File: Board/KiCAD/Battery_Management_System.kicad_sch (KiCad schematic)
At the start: 19 parts, among them J10 Conn_01x02, J11 Conn_01x02, J12 Conn_01x02, J13 Conn_01x02, J5 Conn_01x03, J6 Conn_01x03, J7 Conn_01x05, J8 Conn_01x02, J9 Conn_01x02

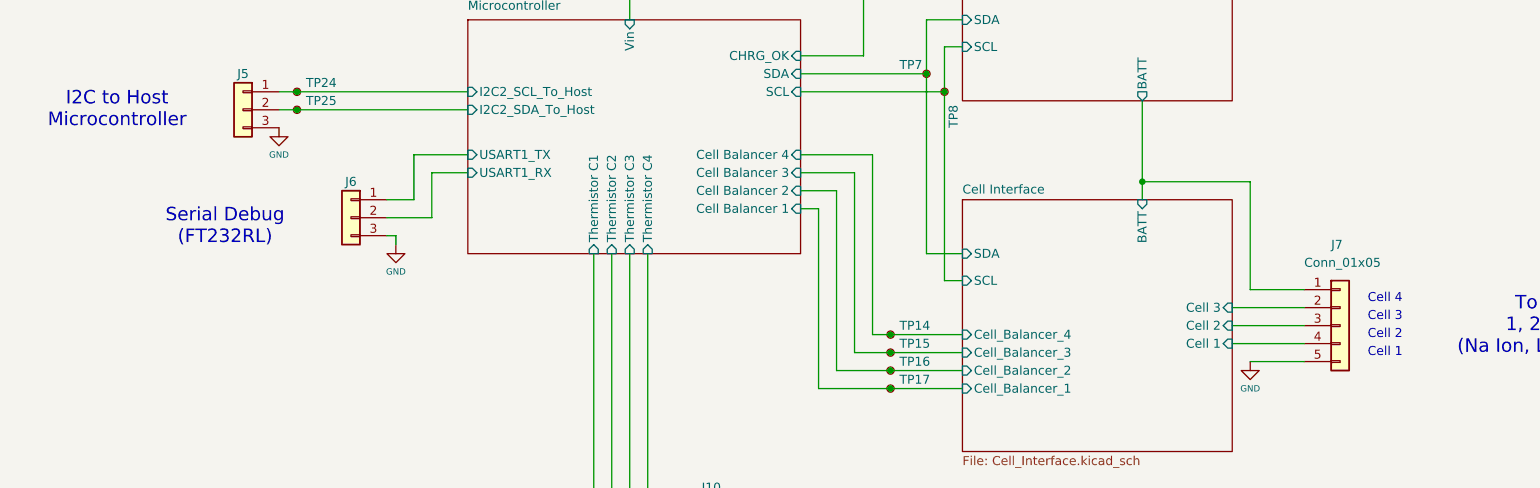
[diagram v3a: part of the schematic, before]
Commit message: Optimized PCB
PCB new dimensions:
43 x 53 mm
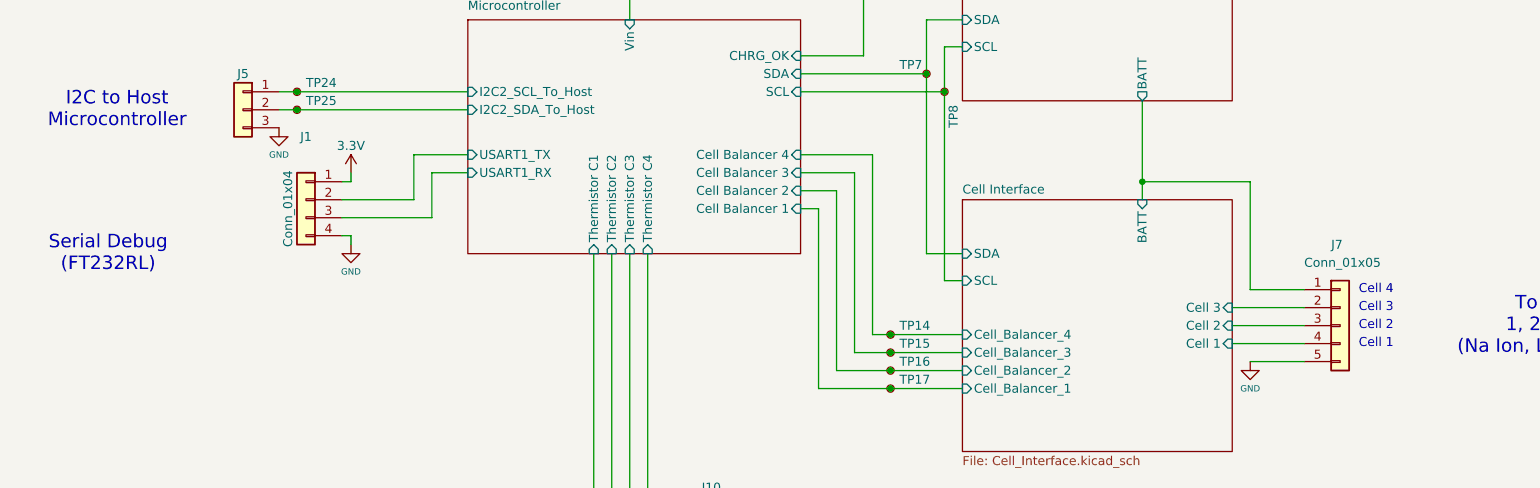
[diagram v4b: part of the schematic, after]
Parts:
- removed J6: Conn_01x03, Connector_PinHeader_2.54mm:PinHeader_1x03_P2.54mm_Vertical, symbol Connector_Generic:Conn_01x03
- added J1: Conn_01x04, Connector_PinHeader_2.54mm:PinHeader_1x04_P2.54mm_Vertical, symbol Connector_Generic:Conn_01x04
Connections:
- net GND: now also J1.4 (Pin_4)
- net Microcontroller/USART1_RX: now also J1.3 (Pin_3)
- net Microcontroller/USART1_TX: now also J1.2 (Pin_2)
- new net 3.3V: J1.1 (Pin_1)
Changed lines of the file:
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@@
 	(text "Cell 3"
 		(exclude_from_sim no)
-		(at 208.28 119.38 0)
+		(at 207.01 118.11 0)
 		(effects
 			(font
@@
 	(text "Cell 4\n"
 		(exclude_from_sim no)
-		(at 208.28 116.84 0)
+		(at 207.01 115.57 0)
 		(effects
 			(font
@@
 	(text "Cell 2"
 		(exclude_from_sim no)
-		(at 208.28 121.92 0)
+		(at 207.01 120.65 0)
 		(effects
 			(font
@@
 	(text "Serial Debug\n(FT232RL)"
 		(exclude_from_sim no)
-		(at 44.45 106.68 0)
+		(at 27.94 110.49 0)
 		(effects
 			(font
@@
 	(text "Cell 1\n"
 		(exclude_from_sim no)
-		(at 208.28 124.46 0)
+		(at 207.01 123.19 0)
 		(effects
 			(font
@@
 	(wire
 		(pts
+			(xy 62.23 99.06) (xy 62.23 100.33)
+		)
+		(stroke
+			(width 0)
+			(type default)
+		)
+	)
+	(wire
+		(pts
 			(xy 189.23 115.57) (xy 189.23 100.33)
 		)
@@
 	(wire
 		(pts
-			(xy 67.31 105.41) (xy 73.66 105.41)
+			(xy 60.96 105.41) (xy 73.66 105.41)
 		)
 		(stroke
@@
 	(wire
 		(pts
-			(xy 68.58 109.22) (xy 68.58 107.95)
+			(xy 62.23 109.22) (xy 62.23 107.95)
 		)
 		(stroke
@@
 	(wire
 		(pts
-			(xy 68.58 107.95) (xy 67.31 107.95)
+			(xy 62.23 107.95) (xy 60.96 107.95)
 		)
 		(stroke
@@
 	(wire
 		(pts
+			(xy 62.23 100.33) (xy 60.96 100.33)
+		)
+		(stroke
+			(width 0)
+			(type default)
+		)
+	)
+	(wire
+		(pts
 			(xy 173.99 88.9) (xy 173.99 100.33)
 		)
@@
 	(wire
 		(pts
-			(xy 67.31 102.87) (xy 71.12 102.87)
+			(xy 60.96 102.87) (xy 71.12 102.87)
 		)
 		(stroke
@@
 	(symbol
 		(lib_id "power:GND")
-		(at 68.58 109.22 0)
+		(at 62.23 109.22 0)
 		(unit 1)
 		(exclude_from_sim no)
@@
 		(dnp no)
 		(property "Reference" "#PWR077"
-			(at 68.58 115.57 0)
+			(at 62.23 115.57 0)
 			(effects
 				(font
@@
 		)
 		(property "Value" "GND"
-			(at 68.58 113.03 0)
+			(at 62.23 113.03 0)
 			(effects
 				(font
@@
 		)
 		(property "Footprint" ""
-			(at 68.58 109.22 0)
+			(at 62.23 109.22 0)
 			(effects
 				(font
@@
 		)
 		(property "Datasheet" ""
-			(at 68.58 109.22 0)
+			(at 62.23 109.22 0)
 			(effects
 				(font
@@
 		)
 		(property "Description" "Power symbol creates a global label with name \"GND\" , ground"
-			(at 68.58 109.22 0)
+			(at 62.23 109.22 0)
 			(effects
 				(font
@@
 	)
 	(symbol
+		(lib_id "Connector_Generic:Conn_01x04")
+		(at 55.88 102.87 0)
+		(mirror y)
+		(unit 1)
+		(exclude_from_sim no)
+		(in_bom yes)
+		(on_board yes)
+		(dnp no)
+		(property "Reference" "J1"
+			(at 55.88 93.98 0)
+			(effects
+				(font
+					(size 1.27 1.27)
+				)
+			)
+		)
+		(property "Value" "Conn_01x04"
+			(at 53.34 104.14 90)
+			(effects
+				(font
+					(size 1.27 1.27)
+				)
+			)
+		)
+		(property "Footprint" "Connector_PinHeader_2.54mm:PinHeader_1x04_P2.54mm_Vertical"
+			(at 55.88 102.87 0)
+			(effects
+				(font
+					(size 1.27 1.27)
+				)
+				(hide yes)
+			)
+		)
+		(property "Datasheet" "~"
+			(at 55.88 102.87 0)
+			(effects
+				(font
+					(size 1.27 1.27)
+				)
+				(hide yes)
+			)
+		)
+		(property "Description" "Generic connector, single row, 01x04, script generated (kicad-library-utils/schlib/autogen/connector/)"
+			(at 55.88 102.87 0)
+			(effects
+				(font
+					(size 1.27 1.27)
+				)
+				(hide yes)
+			)
+		)
+		(pin "3"
+		)
+		(pin "4"
+		)
+		(pin "1"
+		)
+		(pin "2"
+		)
+		(instances
+			(project ""
+				(path "/1ea1a1f5-2618-4570-85b6-e164c8f0e76f"
+					(reference "J1")
+					(unit 1)
+				)
+			)
+		)
+	)
+	(symbol
 		(lib_id "Connector_Generic:Conn_01x02")
 		(at 113.03 146.05 0)
@@
 	)
 	(symbol
-		(lib_id "Connector_Generic:Conn_01x03")
-		(at 62.23 105.41 0)
-		(mirror y)
-		(unit 1)
-		(exclude_from_sim no)
-		(in_bom yes)
-		(on_board yes)
-		(dnp no)
-		(property "Reference" "J6"
-			(at 62.23 100.33 0)
-			(effects
-				(font
-					(size 1.27 1.27)
-				)
-			)
-		)
-		(property "Value" "Conn_01x03"
-			(at 62.23 99.06 0)
-			(effects
-				(font
-					(size 1.27 1.27)
-				)
-				(hide yes)
-			)
-		)
-		(property "Footprint" "Connector_PinHeader_2.54mm:PinHeader_1x03_P2.54mm_Vertical"
-			(at 62.23 105.41 0)
-			(effects
-				(font
-					(size 1.27 1.27)
-				)
-				(hide yes)
-			)
-		)
-		(property "Datasheet" "~"
-			(at 62.23 105.41 0)
-			(effects
-				(font
-					(size 1.27 1.27)
-				)
-				(hide yes)
-			)
-		)
-		(property "Description" "Generic connector, single row, 01x03, script generated (kicad-library-utils/schlib/autogen/connector/)"
-			(at 62.23 105.41 0)
-			(effects
-				(font
-					(size 1.27 1.27)
-				)
-				(hide yes)
-			)
-		)
-		(property "Availability" ""
-			(at 62.23 105.41 0)
-			(effects
-				(font
-					(size 1.27 1.27)
-				)
-			)
-		)
-		(property "Check_prices" ""
-			(at 62.23 105.41 0)
-			(effects
-				(font
-					(size 1.27 1.27)
-				)
-			)
-		)
-		(property "Description_1" ""
-			(at 62.23 105.41 0)
-			(effects
-				(font
-					(size 1.27 1.27)
-				)
-			)
-		)
-		(property "MANUFACTURER" ""
-			(at 62.23 105.41 0)
-			(effects
-				(font
-					(size 1.27 1.27)
-				)
-			)
-		)
-		(property "MAXIMUM_PACKAGE_HEIGHT" ""
-			(at 62.23 105.41 0)
-			(effects
-				(font
-					(size 1.27 1.27)
-				)
-			)
-		)
-		(property "PARTREV" ""
-			(at 62.23 105.41 0)
-			(effects
-				(font
-					(size 1.27 1.27)
-				)
-			)
-		)
-		(property "Package" "61300311121"
-			(at 55.372 112.522 0)
-			(effects
-				(font
-					(size 1.27 1.27)
-				)
-				(hide yes)
-			)
-		)
-		(property "Price" ""
-			(at 62.23 105.41 0)
-			(effects
-				(font
-					(size 1.27 1.27)
-				)
-			)
-		)
-		(property "SNAPEDA_PN" ""
-			(at 62.23 105.41 0)
-			(effects
-				(font
-					(size 1.27 1.27)
-				)
-			)
-		)
-		(property "STANDARD" ""
-			(at 62.23 105.41 0)
-			(effects
-				(font
-					(size 1.27 1.27)
-				)
-			)
-		)
-		(property "SnapEDA_Link" ""
-			(at 62.23 105.41 0)
-			(effects
-				(font
-					(size 1.27 1.27)
-				)
-			)
-		)
-		(property "MFR" "Würth Elektronik"
-			(at 61.468 97.79 0)
-			(effects
-				(font
-					(size 1.27 1.27)
-				)
-				(hide yes)
-			)
-		)
-		(property "MPN" "732-5316-ND"
-			(at 62.23 114.808 0)
-			(effects
-				(font
-					(size 1.27 1.27)
-				)
-				(hide yes)
-			)
-		)
-		(pin "2"
-		)
-		(pin "3"
-		)
-		(pin "1"
-		)
-		(instances
-			(project "Battery_Management_System"
-				(path "/1ea1a1f5-2618-4570-85b6-e164c8f0e76f"
-					(reference "J6")
-					(unit 1)
-				)
-			)
-		)
-	)
-	(symbol
 		(lib_id "Connector_Generic:Conn_01x02")
 		(at 113.03 172.72 0)
@@
 					(unit 1)
 				)
+			)
+		)
+	)
+	(symbol
+		(lib_id "power:VCC")
+		(at 62.23 99.06 0)
+		(unit 1)
+		(exclude_from_sim no)
+		(in_bom yes)
+		(on_board yes)
+		(dnp no)
+		(property "Reference" "#PWR042"
+			(at 62.23 102.87 0)
+			(effects
+				(font
+					(size 1.27 1.27)
+				)
+				(hide yes)
+			)
+		)
+		(property "Value" "3.3V"
+			(at 62.23 95.25 0)
+			(effects
+				(font
+					(size 1.27 1.27)
+				)
+			)
+		)
+		(property "Footprint" ""
+			(at 62.23 99.06 0)
+			(effects
+				(font
+					(size 1.27 1.27)
+				)
+				(hide yes)
+			)
+		)
+		(property "Datasheet" ""
+			(at 62.23 99.06 0)
+			(effects
+				(font
+					(size 1.27 1.27)
+				)
+				(hide yes)
+			)
+		)
+		(property "Description" "Power symbol creates a global label with name \"VCC\""
+			(at 62.23 99.06 0)
+			(effects
+				(font
+					(size 1.27 1.27)
+				)
+				(hide yes)
+			)
+		)
+		(pin "1"
+		)
+		(instances
+			(project "Battery_Management_System"
+				(path "/1ea1a1f5-2618-4570-85b6-e164c8f0e76f"
+					(reference "#PWR042")
+					(unit 1)
+				)

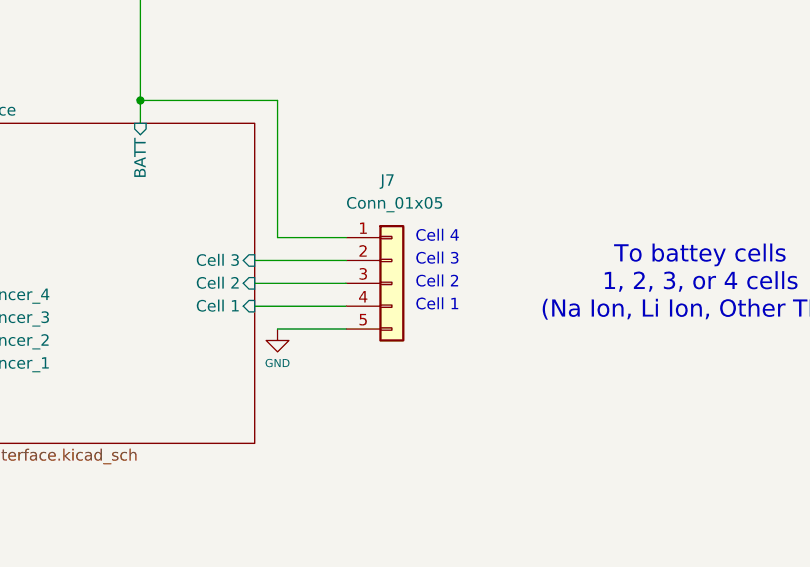
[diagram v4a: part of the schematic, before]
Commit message: Cleaned up BOM materials again. Why do these keep reseting? Also, big refactor on cell balancing circuits and battery connection (NOW FLIPPED) to make board smaller. More smallification is left as an exercise to the reader.
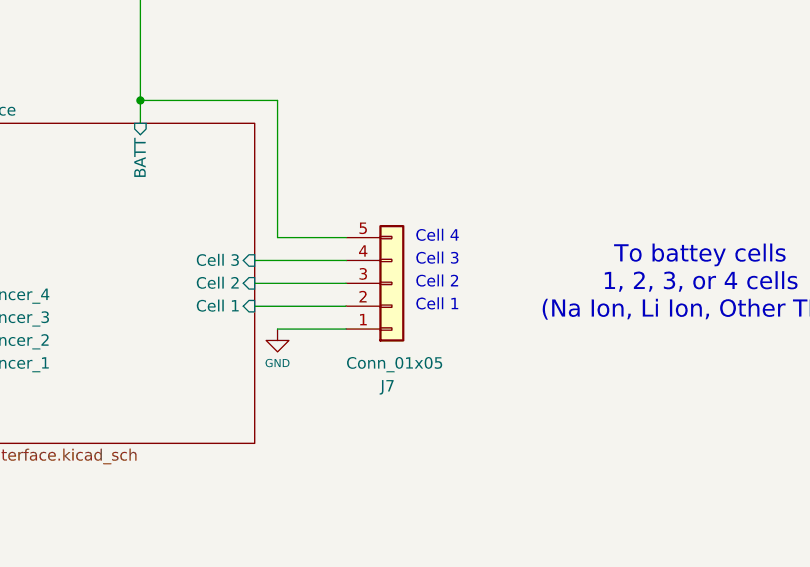
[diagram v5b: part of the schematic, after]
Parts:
- J10, J11, J12, J13, J8, J9: Package 5-146285-2 -> (none)
- J5: Package 61300311121 -> (none)
- J7: Package 61300511121 -> (none)
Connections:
- net Cell Interface/BATT: now also J7.5 (Pin_5); no longer J7.1 (Pin_1)
- net Cell Interface/Cell 1: now also J7.2 (Pin_2); no longer J7.4 (Pin_4)
- net Cell Interface/Cell 3: now also J7.4 (Pin_4); no longer J7.2 (Pin_2)
- net GND: now also J7.1 (Pin_1); no longer J7.5 (Pin_5)

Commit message: EPL - Battery Management System REV 2
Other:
- note added: "10K NTC Thermistor Cell 2"
- note added: "10K NTC Thermistor Cell 3"
- note added: "10K NTC Thermistor Cell 4"
- note added: "Blinking LED: Fast blinking for fast charging / high current slow blinking for slow charging \ low current static / fully charged gpio connected"
- note added: "Error LED: something went wrong"
- note added: "Status LED: Am I fully CHarged?"
- note added: "Status LED: Do I have power coming in?"
- moved on the sheet: J10, J11, J12, J13

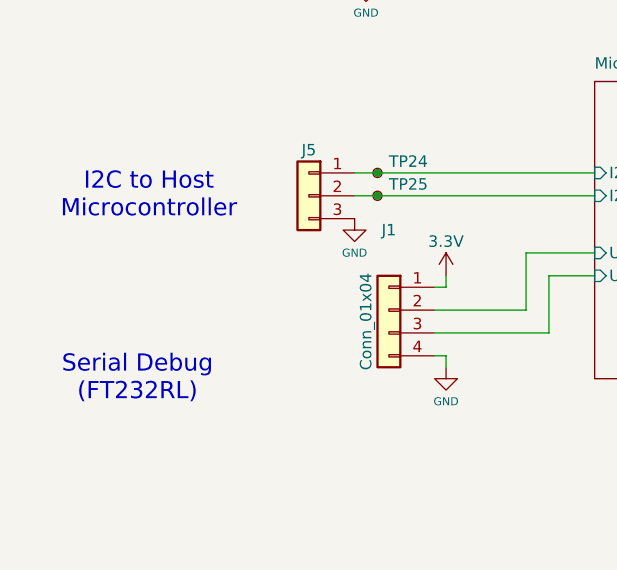
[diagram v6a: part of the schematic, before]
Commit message: Revision to the board
@andrewgreenberg added ground vias near the components needing ground
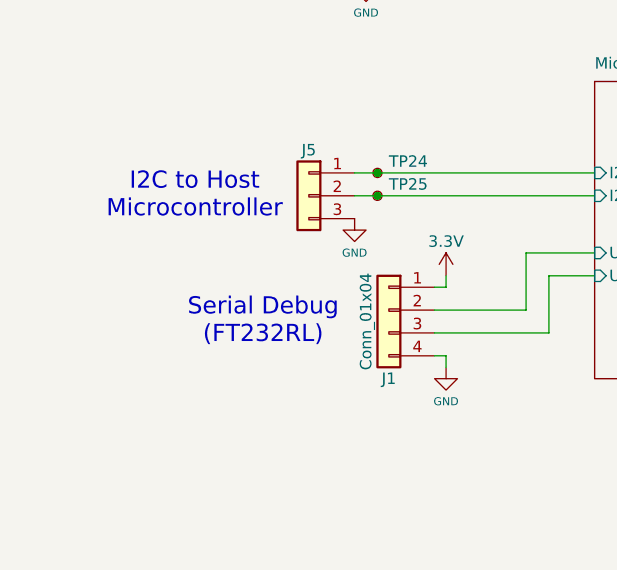
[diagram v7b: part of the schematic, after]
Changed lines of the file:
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@@
 	(text "I2C to Host \nMicrocontroller"
 		(exclude_from_sim no)
-		(at 29.21 90.17 0)
+		(at 34.29 90.17 0)
 		(effects
 			(font
@@
 	(text "Serial Debug\n(FT232RL)"
 		(exclude_from_sim no)
-		(at 27.94 110.49 0)
+		(at 41.91 104.14 0)
 		(effects
 			(font
@@
 		(dnp no)
 		(property "Reference" "J1"
-			(at 55.88 93.98 0)
-			(effects
-				(font
+			(at 55.88 110.49 0)
+			(effects
+				(font

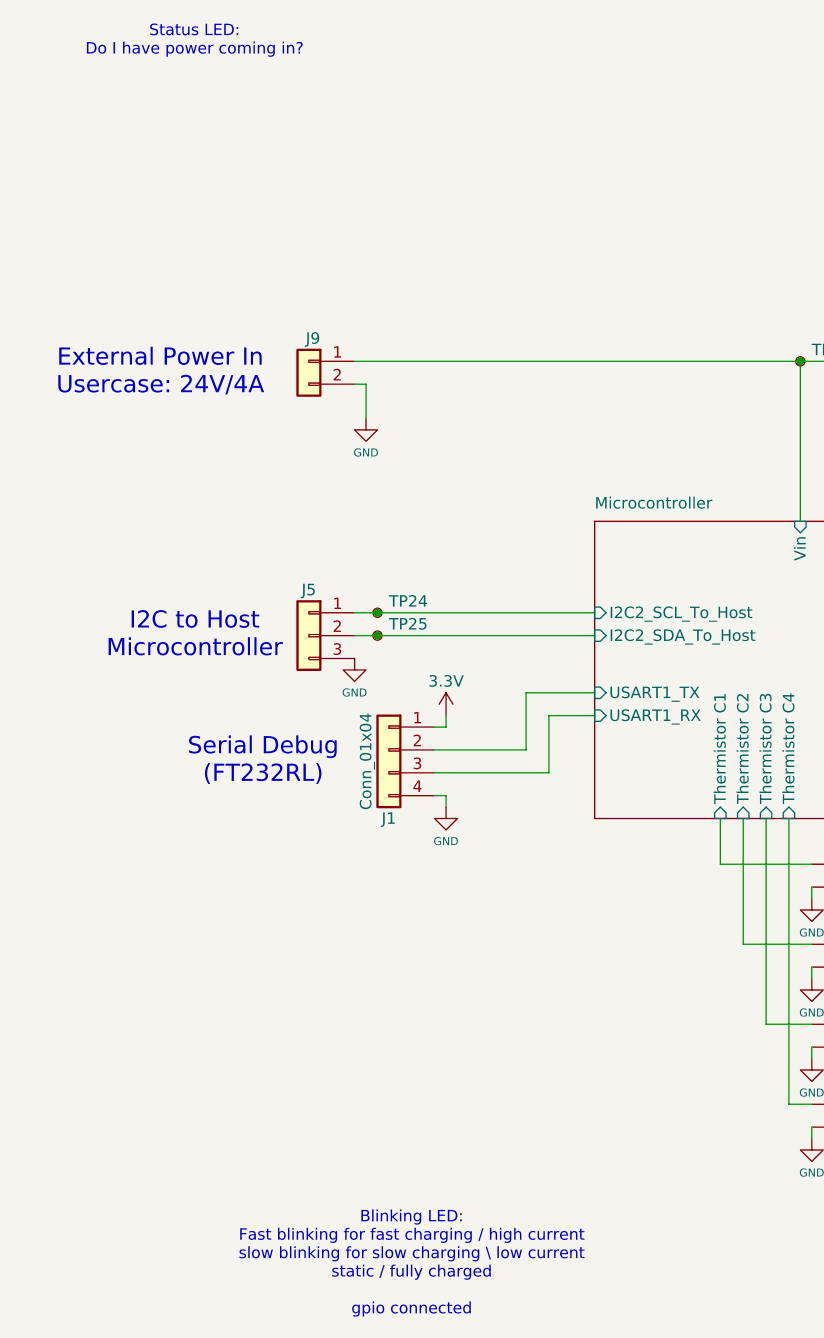
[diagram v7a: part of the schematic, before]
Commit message: PCB with updated Footprint for LTC
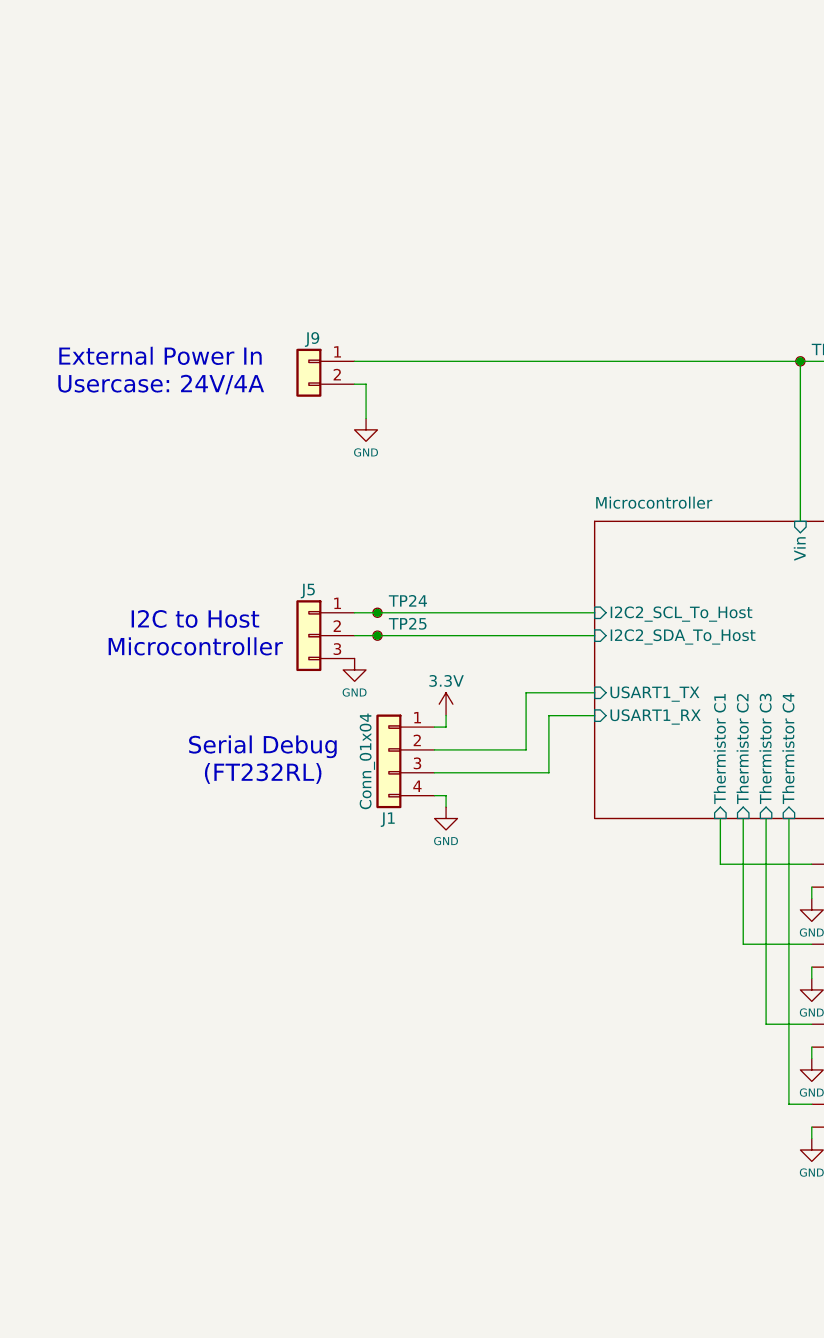
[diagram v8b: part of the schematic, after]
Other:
- note removed: "Blinking LED: Fast blinking for fast charging / high current slow blinking for slow charging \ low current static / fully charged gpio connected"
- note removed: "Status LED: Do I have power coming in?"
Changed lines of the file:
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@@
-		)
-	)
-	(text "Status LED:\nDo I have power coming in?\n"
-		(exclude_from_sim no)
-		(at 34.29 24.13 0)
-		(effects
-			(font
-				(size 1.27 1.27)
-			)
 		)
 	)
@@
 		(effects
 			(font
-				(size 1.27 1.27)
-			)
-		)
-	)
-	(text "Blinking LED:\nFast blinking for fast charging / high current\nslow blinking for slow charging \\ low current\nstatic / fully charged\n\ngpio connected"
-		(exclude_from_sim no)
-		(at 58.42 160.02 0)
-		(effects
-			(font
